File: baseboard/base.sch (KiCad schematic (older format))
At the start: 39 parts, among them J1 Conn_02x05_Odd_Even, J2 Barrel_Jack, J3 Barrel_Jack, J4 Conn_01x03_Male, Q1 BSS138, Q2 BSS138, Q3 BSS138, Q4 BSS138, Q5 BSS138, Q6 BSS138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

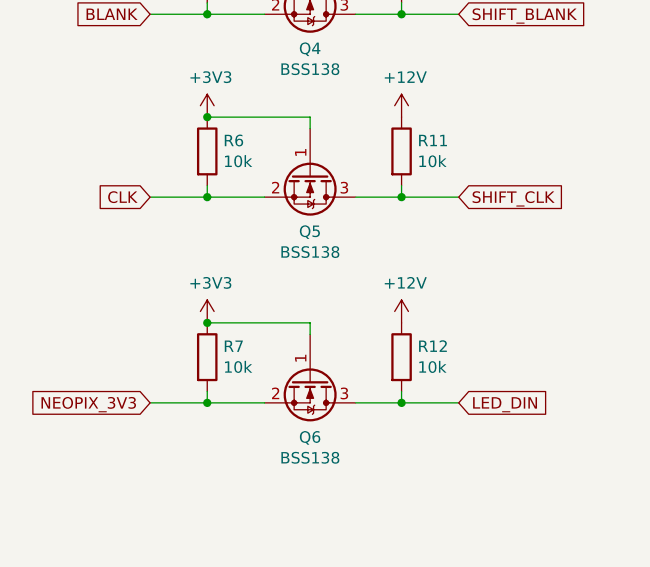
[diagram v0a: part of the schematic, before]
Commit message: Fix LED level shifter - should be to +5V, not +12V...
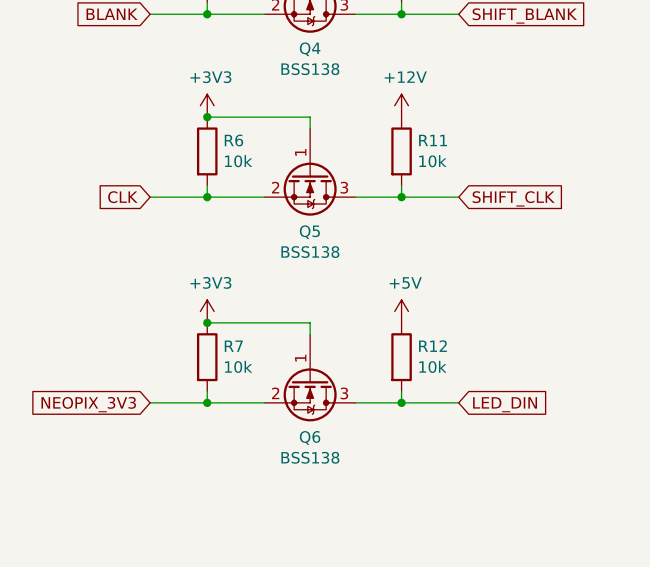
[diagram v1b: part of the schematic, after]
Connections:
- net +12V: no longer R12.1
- net +5V: now also R12.1
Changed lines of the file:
@@
-$EndComp
-$Comp
-L power:+12V #PWR0121
-U 1 1 5DA2481D
-P 10100 5800
-F 0 "#PWR0121" H 10100 5650 50  0001 C CNN
-F 1 "+12V" H 10115 5973 50  0000 C CNN
-F 2 "" H 10100 5800 50  0001 C CNN
-F 3 "" H 10100 5800 50  0001 C CNN
-	1    10100 5800
-	1    0    0    -1
 $EndComp
 $Comp
@@
 Text GLabel 5650 5900 2    50   Input ~ 0
 SW_3
+$Comp
+L power:+5V #PWR?
+U 1 1 5DCB14D8
+P 10100 5800
+F 0 "#PWR?" H 10100 5650 50  0001 C CNN
+F 1 "+5V" H 10115 5973 50  0000 C CNN
+F 2 "" H 10100 5800 50  0001 C CNN
+F 3 "" H 10100 5800 50  0001 C CNN
+	1    10100 5800
+	1    0    0    -1
+$EndComp
 $EndSCHEMATC

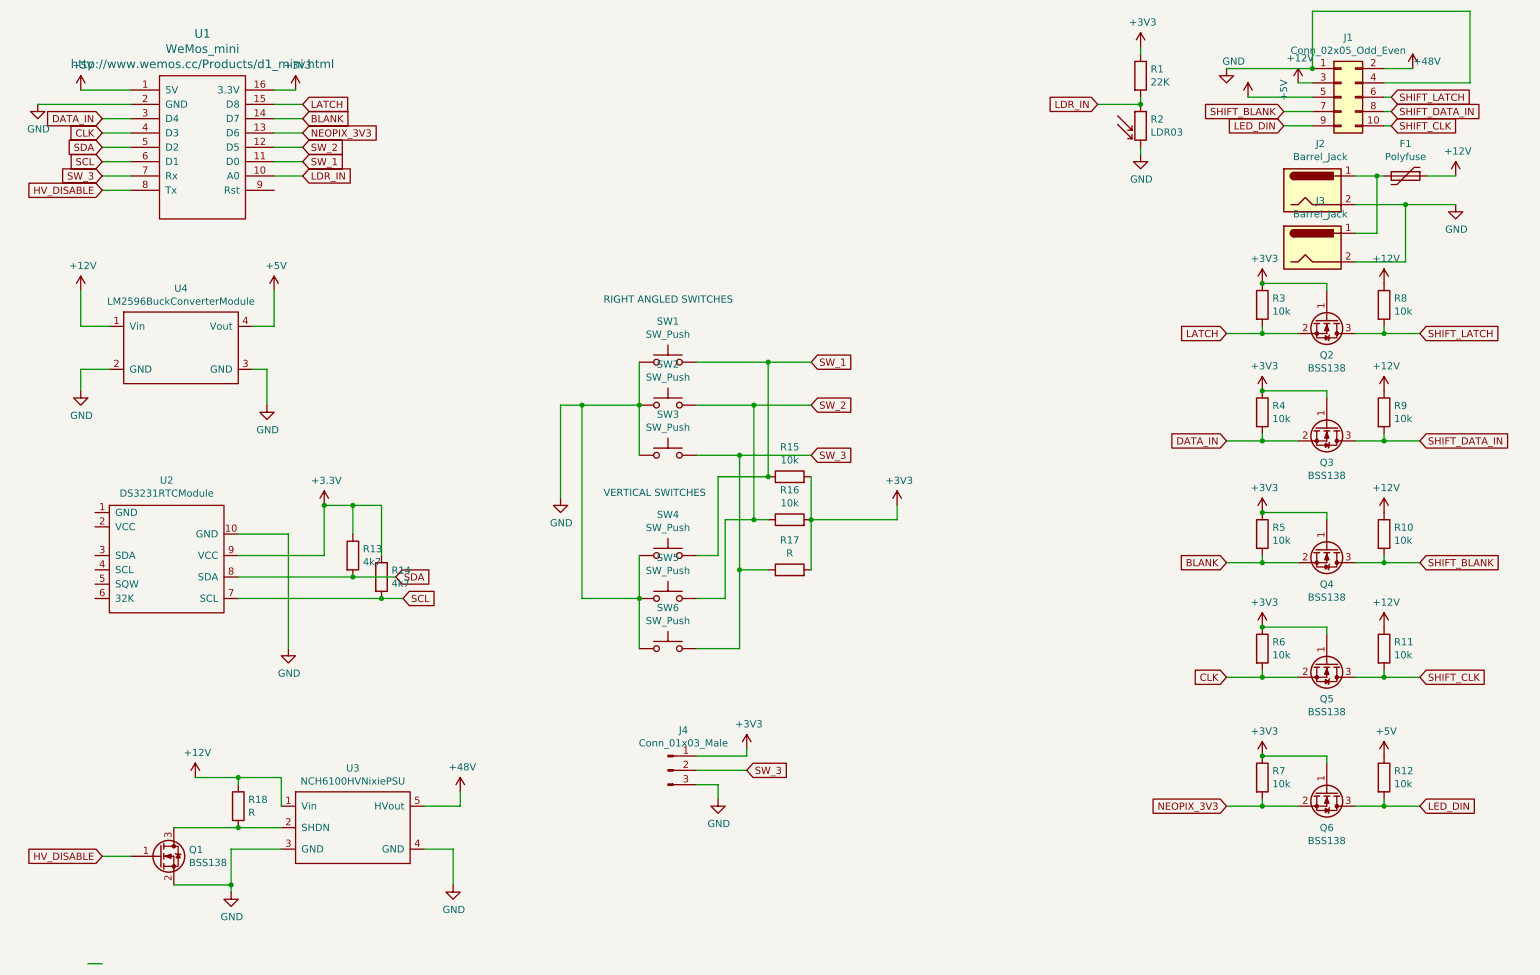
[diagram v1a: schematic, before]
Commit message: Remove LED level shifter (using diodes on tube 'boards'), so not needed. Rejig GPIOs as wemos won't boot if D8 is pulled HIGH (and the level shifter *did* pull it high)
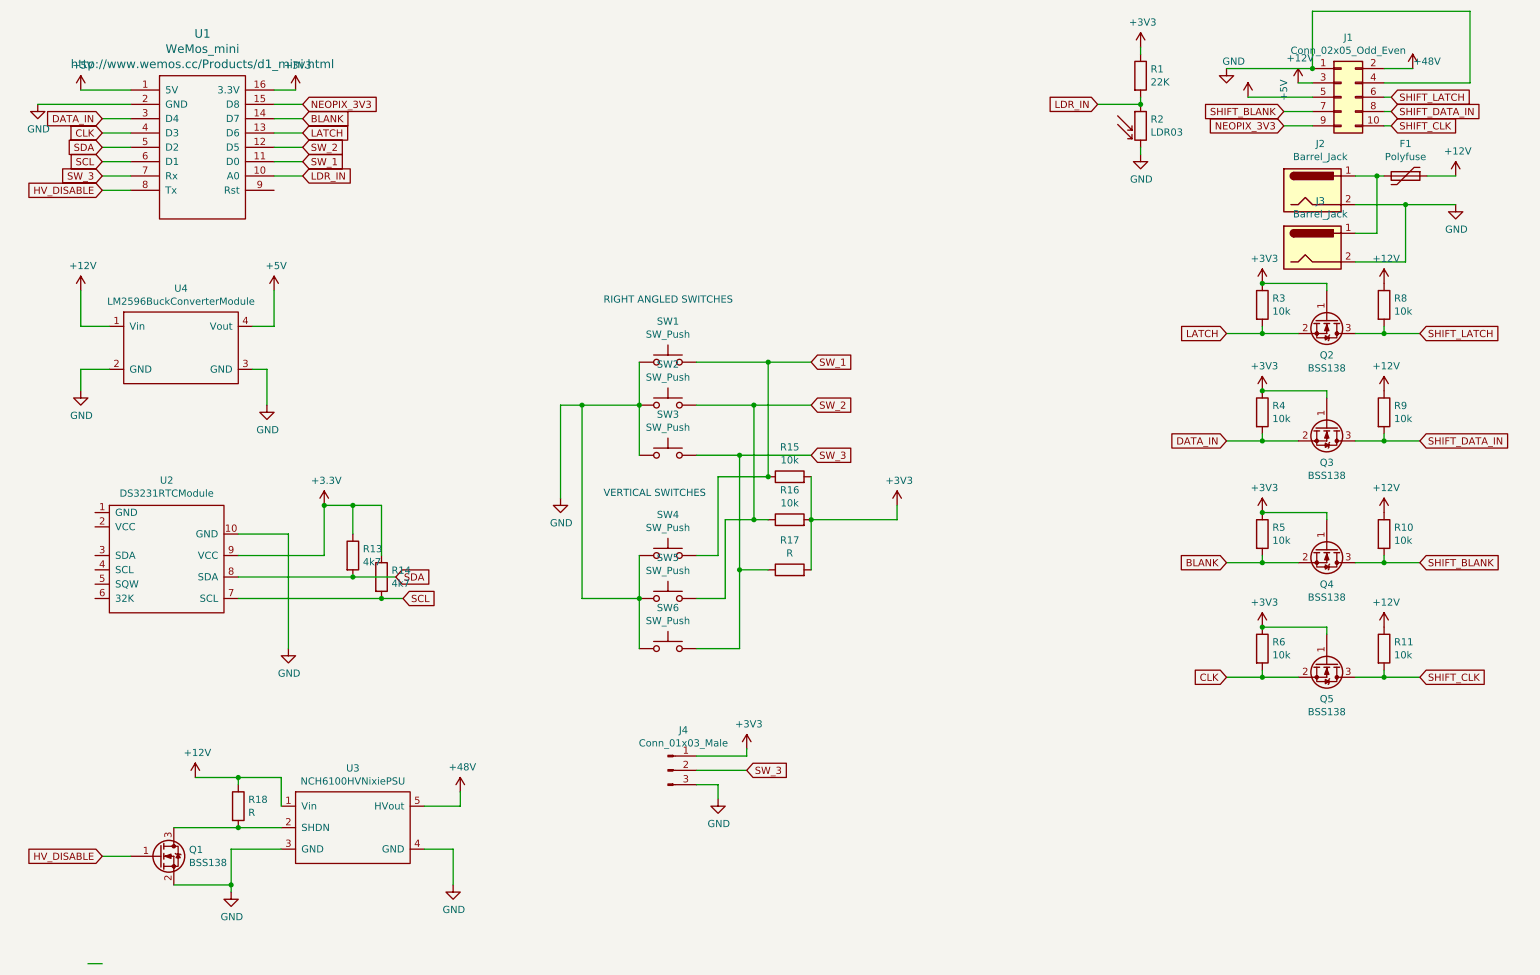
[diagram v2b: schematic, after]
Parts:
- removed Q6: BSS138, Package_TO_SOT_SMD:SOT-23, symbol Transistor_FET:BSS138
- removed R12, R7: 10k, Resistor_SMD:R_0805_2012Metric_Pad1.15x1.40mm_HandSolder, symbol Device:R
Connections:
- net LED_DIN is gone; now on net NEOPIX_3V3: J1.9 (Pin_9)
- net LATCH: now also U1.13 (D6); no longer U1.15 (D8)
- net NEOPIX_3V3: now also U1.15 (D8); no longer U1.13 (D6)
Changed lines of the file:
@@
 Wire Wire Line
 	9400 1400 9600 1400
-Text GLabel 9400 1400 0    50   Input ~ 0
-LED_DIN
 Text GLabel 10150 1400 2    50   Input ~ 0
 SHIFT_CLK
@@
 Wire Wire Line
 	2350 1450 2550 1450
-Text GLabel 2550 1450 2    50   Input ~ 0
+Text GLabel 2550 1250 2    50   Input ~ 0
 NEOPIX_3V3
 Wire Wire Line
@@
 Text GLabel 9000 5250 0    50   Input ~ 0
 CLK
-Text GLabel 2550 1250 2    50   Input ~ 0
-LATCH
 Text GLabel 2550 1350 2    50   Input ~ 0
 BLANK
@@
 Wire Wire Line
 	1350 1850 1150 1850
-Text GLabel 2550 1550 2    50   Input ~ 0
-SW_2
 Text GLabel 2550 1650 2    50   Input ~ 0
 SW_1
 Text GLabel 1150 1750 0    50   Input ~ 0
 SW_3
-$Comp
-L power:+3V3 #PWR0120
-U 1 1 5DA24817
-P 9250 5800
-F 0 "#PWR0120" H 9250 5650 50  0001 C CNN
-F 1 "+3V3" H 9265 5973 50  0000 C CNN
-F 2 "" H 9250 5800 50  0001 C CNN
-F 3 "" H 9250 5800 50  0001 C CNN
-	1    9250 5800
-	1    0    0    -1
-$EndComp
-$Comp
-L Device:R R7
-U 1 1 5DA24823
-P 9250 5950
-F 0 "R7" H 9320 5996 50  0000 L CNN
-F 1 "10k" H 9320 5905 50  0000 L CNN
-F 2 "Resistor_SMD:R_0805_2012Metric_Pad1.15x1.40mm_HandSolder" V 9180 5950 50  0001 C CNN
-F 3 "~" H 9250 5950 50  0001 C CNN
-	1    9250 5950
-	1    0    0    -1
-$EndComp
-Wire Wire Line
-	9250 6100 9250 6150
-Wire Wire Line
-	9250 6150 9500 6150
-$Comp
-L Device:R R12
-U 1 1 5DA2482C
-P 10100 5950
-F 0 "R12" H 10170 5996 50  0000 L CNN
-F 1 "10k" H 10170 5905 50  0000 L CNN
-F 2 "Resistor_SMD:R_0805_2012Metric_Pad1.15x1.40mm_HandSolder" V 10030 5950 50  0001 C CNN
-F 3 "~" H 10100 5950 50  0001 C CNN
-	1    10100 5950
-	1    0    0    -1
-$EndComp
-Wire Wire Line
-	10100 6100 10100 6150
-Wire Wire Line
-	10100 6150 9900 6150
-Wire Wire Line
-	9250 5800 9700 5800
-Wire Wire Line
-	9700 5800 9700 5850
-Connection ~ 9250 5800
-Wire Wire Line
-	10100 6150 10350 6150
-Connection ~ 10100 6150
-Wire Wire Line
-	9250 6150 9000 6150
-Connection ~ 9250 6150
-Text GLabel 10350 6150 2    50   Input ~ 0
-LED_DIN
-Text GLabel 9000 6150 0    50   Input ~ 0
+Text GLabel 9400 1400 0    50   Input ~ 0
 NEOPIX_3V3
 Text GLabel 1150 1850 0    50   Input ~ 0
@@
 	0    1    1    0
 $EndComp
-$Comp
-L Transistor_FET:BSS138 Q6
-U 1 1 5DDA2457
-P 9700 6050
-F 0 "Q6" V 9951 6050 50  0000 C CNN
-F 1 "BSS138" V 10042 6050 50  0000 C CNN
-F 2 "Package_TO_SOT_SMD:SOT-23" H 9900 5975 50  0001 L CIN
-F 3 "https://www.fairchildsemi.com/datasheets/BS/BSS138.pdf" H 9700 6050 50  0001 L CNN
-	1    9700 6050
-	0    1    1    0
-$EndComp
 Wire Wire Line
 	5300 3050 5800 3050
@@
 Text GLabel 5650 5900 2    50   Input ~ 0
 SW_3
-$Comp
-L power:+5V #PWR?
-U 1 1 5DCB14D8
-P 10100 5800
-F 0 "#PWR?" H 10100 5650 50  0001 C CNN
-F 1 "+5V" H 10115 5973 50  0000 C CNN
-F 2 "" H 10100 5800 50  0001 C CNN
-F 3 "" H 10100 5800 50  0001 C CNN
-	1    10100 5800
-	1    0    0    -1
-$EndComp
+Text GLabel 2550 1450 2    50   Input ~ 0
+LATCH
+Text GLabel 2550 1550 2    50   Input ~ 0
+SW_2
 $EndSCHEMATC

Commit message: Add pullup resistor to switching FET for HVPSU Remove I2C pullups (they aren't needed, as the RTC module has built in pullups)
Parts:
- removed R13, R14: 4k7, Resistor_THT:R_Axial_DIN0309_L9.0mm_D3.2mm_P12.70mm_Horizontal, symbol Device:R
- added R7: 10K, Resistor_SMD:R_0805_2012Metric_Pad1.15x1.40mm_HandSolder, symbol Device:R
- U2: symbol GenericModules:DS3231RTCModule -> base-rescue:DS3231RTCModule-GenericModules
- U3: symbol GenericModules:NCH6100HVNixiePSU -> base-rescue:NCH6100HVNixiePSU-GenericModules
- U4: symbol GenericModules:LM2596BuckConverterModule -> base-rescue:LM2596BuckConverterModule-GenericModules
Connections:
- net +3V3: now also R7.1
- net HV_DISABLE: now also R7.2
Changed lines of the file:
@@
 Wire Wire Line
 	2100 4250 2450 4250
-Wire Wire Line
-	2100 4550 2900 4550
-Wire Wire Line
-	2100 4700 3100 4700
-$Comp
-L Device:R R13
-U 1 1 5DC18026
-P 2900 4400
-F 0 "R13" H 2970 4446 50  0000 L CNN
-F 1 "4k7" H 2970 4355 50  0000 L CNN
-F 2 "Resistor_THT:R_Axial_DIN0309_L9.0mm_D3.2mm_P12.70mm_Horizontal" V 2830 4400 50  0001 C CNN
-F 3 "~" H 2900 4400 50  0001 C CNN
-	1    2900 4400
-	1    0    0    -1
-$EndComp
-Connection ~ 2900 4550
-Wire Wire Line
-	2900 4550 3200 4550
-$Comp
-L Device:R R14
-U 1 1 5DC18940
-P 3100 4550
-F 0 "R14" H 3170 4596 50  0000 L CNN
-F 1 "4k7" H 3170 4505 50  0000 L CNN
-F 2 "Resistor_THT:R_Axial_DIN0309_L9.0mm_D3.2mm_P12.70mm_Horizontal" V 3030 4550 50  0001 C CNN
-F 3 "~" H 3100 4550 50  0001 C CNN
-	1    3100 4550
-	1    0    0    -1
-$EndComp
-Connection ~ 3100 4700
-Wire Wire Line
-	3100 4700 3250 4700
-Wire Wire Line
-	2900 4250 2900 4050
-Wire Wire Line
-	2900 4050 2700 4050
-Connection ~ 2700 4050
-Wire Wire Line
-	2900 4050 3100 4050
-Wire Wire Line
-	3100 4050 3100 4400
-Connection ~ 2900 4050
-$Comp
-L GenericModules:NCH6100HVNixiePSU U3
+$Comp
+L base-rescue:NCH6100HVNixiePSU-GenericModules U3
 U 1 1 5DC2EC46
 P 2850 6350
@@
 $EndComp
 $Comp
-L GenericModules:DS3231RTCModule U2
+L base-rescue:DS3231RTCModule-GenericModules U2
 U 1 1 5DC2F9CB
 P 1600 4400
@@
 $EndComp
 $Comp
-L GenericModules:LM2596BuckConverterModule U4
+L base-rescue:LM2596BuckConverterModule-GenericModules U4
 U 1 1 5DC32624
 P 1650 3000
@@
 	2050 6700 2050 6750
 Wire Wire Line
-	1050 7250 1150 7250
-$Comp
-L Transistor_FET:BSS138 Q1
-U 1 1 5DD75B39
-P 1550 6500
-F 0 "Q1" H 1756 6546 50  0000 L CNN
-F 1 "BSS138" H 1756 6455 50  0000 L CNN
-F 2 "Package_TO_SOT_SMD:SOT-23" H 1750 6425 50  0001 L CIN
-F 3 "https://www.fairchildsemi.com/datasheets/BS/BSS138.pdf" H 1550 6500 50  0001 L CNN
-	1    1550 6500
-	1    0    0    -1
-$EndComp
-Wire Wire Line
 	1150 6500 1350 6500
 $Comp
@@
 Text GLabel 2550 1550 2    50   Input ~ 0
 SW_2
+$Comp
+L Device:R R7
+U 1 1 5DE5FC03
+P 1350 6200
+F 0 "R7" H 1420 6246 50  0000 L CNN
+F 1 "10K" H 1420 6155 50  0000 L CNN
+F 2 "Resistor_SMD:R_0805_2012Metric_Pad1.15x1.40mm_HandSolder" V 1280 6200 50  0001 C CNN
+F 3 "~" H 1350 6200 50  0001 C CNN
+	1    1350 6200
+	1    0    0    -1
+$EndComp
+$Comp
+L power:+3V3 #PWR0120
+U 1 1 5DE60E59
+P 1350 5950
+F 0 "#PWR0120" H 1350 5800 50  0001 C CNN
+F 1 "+3V3" H 1365 6123 50  0000 C CNN
+F 2 "" H 1350 5950 50  0001 C CNN
+F 3 "" H 1350 5950 50  0001 C CNN
+	1    1350 5950
+	1    0    0    -1
+$EndComp
+$Comp
+L Transistor_FET:BSS138 Q1
+U 1 1 5DD75B39
+P 1550 6500
+F 0 "Q1" H 1756 6546 50  0000 L CNN
+F 1 "BSS138" H 1756 6455 50  0000 L CNN
+F 2 "Package_TO_SOT_SMD:SOT-23" H 1750 6425 50  0001 L CIN
+F 3 "https://www.fairchildsemi.com/datasheets/BS/BSS138.pdf" H 1550 6500 50  0001 L CNN
+	1    1550 6500
+	1    0    0    -1
+$EndComp
+Wire Wire Line
+	1350 6050 1350 5950
+Wire Wire Line
+	1350 6350 1350 6500
+Connection ~ 1350 6500
+Wire Wire Line
+	2100 4700 3250 4700
+Wire Wire Line
+	2100 4550 3200 4550
 $EndSCHEMATC

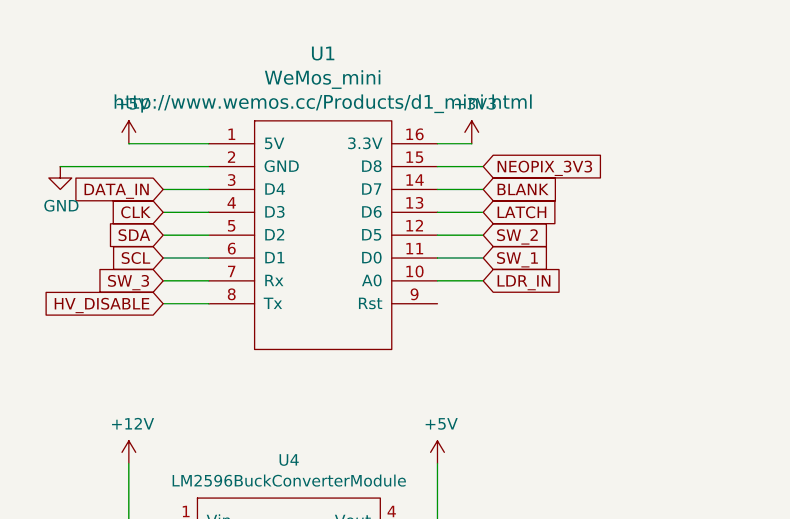
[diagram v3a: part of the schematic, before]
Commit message: More refactoring of ESP8266 pinout issues to ensure booting functions correctly
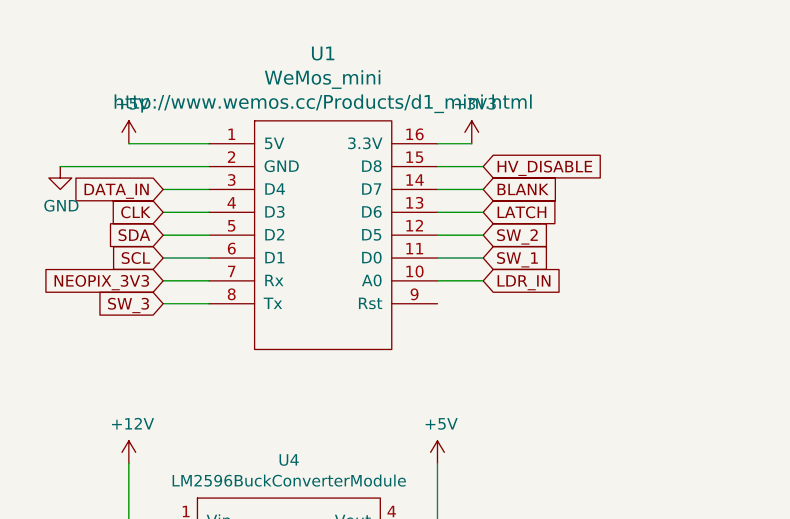
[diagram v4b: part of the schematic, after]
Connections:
- net HV_DISABLE: now also U1.15 (D8); no longer U1.8 (Tx)
- net NEOPIX_3V3: now also U1.7 (Rx); no longer U1.15 (D8)
- net SW_3: now also U1.8 (Tx); no longer U1.7 (Rx)
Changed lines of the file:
@@
 Wire Wire Line
 	2350 1450 2550 1450
-Text GLabel 2550 1250 2    50   Input ~ 0
+Text GLabel 1150 1750 0    50   Input ~ 0
 NEOPIX_3V3
 Wire Wire Line
@@
 Text GLabel 2550 1650 2    50   Input ~ 0
 SW_1
-Text GLabel 1150 1750 0    50   Input ~ 0
+Text GLabel 1150 1850 0    50   Input ~ 0
 SW_3
 Text GLabel 9400 1400 0    50   Input ~ 0
 NEOPIX_3V3
-Text GLabel 1150 1850 0    50   Input ~ 0
+Text GLabel 2550 1250 2    50   Input ~ 0
 HV_DISABLE
 $Comp

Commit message: Fix pulldown
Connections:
- net +3V3: no longer R7.1
- net GND: now also R7.2
- net HV_DISABLE: now also R7.1; no longer R7.2
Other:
- moved on the sheet: R7
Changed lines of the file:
@@
 L power:GND #PWR0130
 U 1 1 5DC41A7F
-P 2050 6750
-F 0 "#PWR0130" H 2050 6500 50  0001 C CNN
-F 1 "GND" H 2055 6577 50  0000 C CNN
-F 2 "" H 2050 6750 50  0001 C CNN
-F 3 "" H 2050 6750 50  0001 C CNN
-	1    2050 6750
+P 2050 6850
+F 0 "#PWR0130" H 2050 6600 50  0001 C CNN
+F 1 "GND" H 2055 6677 50  0000 C CNN
+F 2 "" H 2050 6850 50  0001 C CNN
+F 3 "" H 2050 6850 50  0001 C CNN
+	1    2050 6850
 	1    0    0    -1
 $EndComp
@@
 	1650 6700 2050 6700
 Connection ~ 2050 6700
-Wire Wire Line
-	2050 6700 2050 6750
-Wire Wire Line
-	1150 6500 1350 6500
 $Comp
 L Transistor_FET:BSS138 Q5
@@
 Text GLabel 2550 1550 2    50   Input ~ 0
 SW_2
-$Comp
-L Device:R R7
-U 1 1 5DE5FC03
-P 1350 6200
-F 0 "R7" H 1420 6246 50  0000 L CNN
-F 1 "10K" H 1420 6155 50  0000 L CNN
-F 2 "Resistor_SMD:R_0805_2012Metric_Pad1.15x1.40mm_HandSolder" V 1280 6200 50  0001 C CNN
-F 3 "~" H 1350 6200 50  0001 C CNN
-	1    1350 6200
-	1    0    0    -1
-$EndComp
-$Comp
-L power:+3V3 #PWR0120
-U 1 1 5DE60E59
-P 1350 5950
-F 0 "#PWR0120" H 1350 5800 50  0001 C CNN
-F 1 "+3V3" H 1365 6123 50  0000 C CNN
-F 2 "" H 1350 5950 50  0001 C CNN
-F 3 "" H 1350 5950 50  0001 C CNN
-	1    1350 5950
-	1    0    0    -1
-$EndComp
+Wire Wire Line
+	2100 4700 3250 4700
+Wire Wire Line
+	2100 4550 3200 4550
 $Comp
 L Transistor_FET:BSS138 Q1
@@
 $EndComp
 Wire Wire Line
-	1350 6050 1350 5950
-Wire Wire Line
-	1350 6350 1350 6500
-Connection ~ 1350 6500
-Wire Wire Line
-	2100 4700 3250 4700
-Wire Wire Line
-	2100 4550 3200 4550
+	1150 6500 1300 6500
+$Comp
+L Device:R R7
+U 1 1 5DE5FC03
+P 1300 6650
+F 0 "R7" H 1370 6696 50  0000 L CNN
+F 1 "10K" H 1370 6605 50  0000 L CNN
+F 2 "Resistor_SMD:R_0805_2012Metric_Pad1.15x1.40mm_HandSolder" V 1230 6650 50  0001 C CNN
+F 3 "~" H 1300 6650 50  0001 C CNN
+	1    1300 6650
+	1    0    0    -1
+$EndComp
+Wire Wire Line
+	2050 6700 2050 6800
+Connection ~ 1300 6500
+Wire Wire Line
+	1300 6500 1350 6500
+Wire Wire Line
+	1300 6800 2050 6800
+Connection ~ 2050 6800
+Wire Wire Line
+	2050 6800 2050 6850
 $EndSCHEMATC
